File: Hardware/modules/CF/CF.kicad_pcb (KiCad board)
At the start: 4 copper layers, 83.3 x 68.2 mm, 20 parts, among them J1 CF Card, J2 Bus_PCI_6502, U1 74HC00, U2 74LS32, U3 74HCT74, U4 74HC138

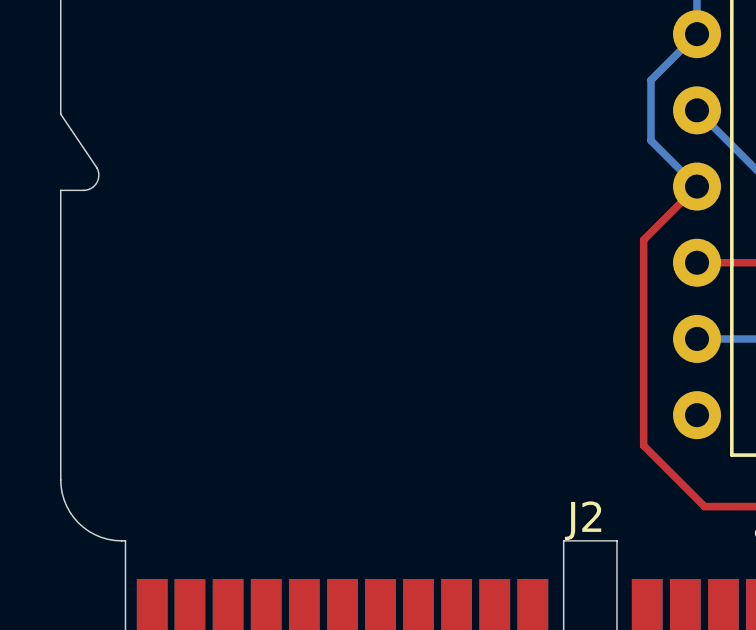
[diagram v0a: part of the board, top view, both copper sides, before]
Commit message: Hardware Review Pt. 1 fix Address Decoding for Strobe Generators add bulk capacitance to every board fix wiring of Prototyping Board
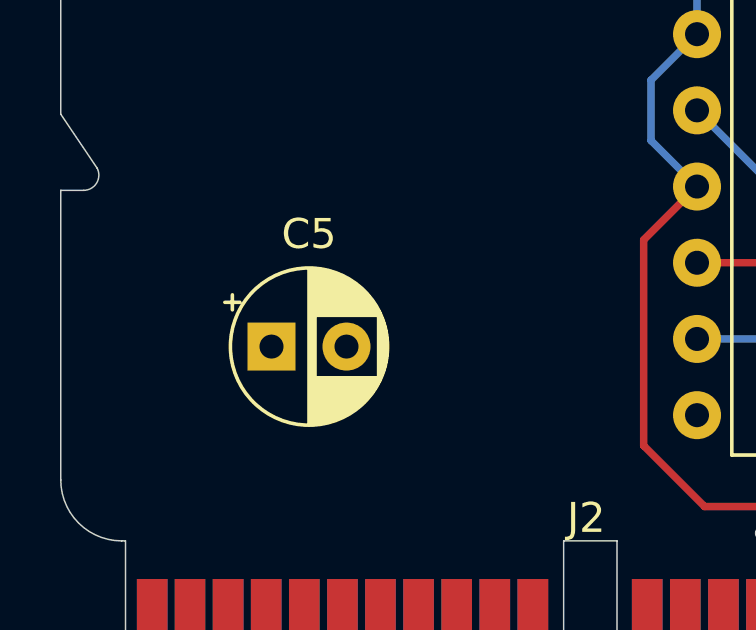
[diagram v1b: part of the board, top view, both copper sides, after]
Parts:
- added C5: C_Polarized, Capacitor_THT:CP_Radial_D5.0mm_P2.50mm, F.Cu at (106.5, 112.3)
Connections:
- J2 pad A11: /A13 -> unconnected-(J2-A13-PadA11)_0
- J2 pad A12: /A15 -> unconnected-(J2-A15-PadA12)
- J2 pad A25: /~{ROM} -> unconnected-(J2-~{ROM}-PadA25)_0
- J2 pad A27: /~{IRQ_0.0} -> unconnected-(J2-~{IRQ_0.0}-PadA27)_0
- J2 pad A28: /~{IRQ_0.1} -> unconnected-(J2-~{IRQ_0.1}-PadA28)_0
- J2 pad A29: /~{IRQ_0.2} -> unconnected-(J2-~{IRQ_0.2}-PadA29)_0
- J2 pad A30: /~{IRQ_0.3} -> unconnected-(J2-~{IRQ_0.3}-PadA30)_0
- J2 pad A31: /~{IRQ_0.4} -> unconnected-(J2-~{IRQ_0.4}-PadA31)_0
- J2 pad A32: /~{IRQ_0.5} -> unconnected-(J2-~{IRQ_0.5}-PadA32)_0
- J2 pad A33: /~{IRQ_0.6} -> unconnected-(J2-~{IRQ_0.6}-PadA33)
- J2 pad A34: /~{IRQ_0.7} -> unconnected-(J2-~{IRQ_0.7}-PadA34)
- J2 pad A38: /SYNC_VPA -> unconnected-(J2-Sync/VPA-PadA38)_0
- J2 pad A39: /Ø2/VDA -> unconnected-(J2-Ø2/VDA-PadA39)_0
- J2 pad A41: /~{RDY} -> unconnected-(J2-~{RDY}-PadA41)
- J2 pad A42: /~{BE} -> unconnected-(J2-~{BE}-PadA42)
- J2 pad A45: /E -> unconnected-(J2-E-PadA45)_0
- J2 pad A53: /RAM_0 -> unconnected-(J2-RAM0-PadA53)_0
- J2 pad A54: /RAM_1 -> unconnected-(J2-RAM1-PadA54)
- J2 pad A55: /RAM_2 -> unconnected-(J2-RAM2-PadA55)_0
- J2 pad A56: /RAM_3 -> unconnected-(J2-RAM3-PadA56)
- J2 pad A58: /RAM_4 -> unconnected-(J2-RAM4-PadA58)_0
- J2 pad A59: /RAM_5 -> unconnected-(J2-RAM5-PadA59)
- J2 pad A60: /RAM_6 -> unconnected-(J2-RAM6-PadA60)_0
- J2 pad A61: /RAM_7 -> unconnected-(J2-RAM7-PadA61)
- J2 pad A8: /A9 -> unconnected-(J2-A9-PadA8)_0
- J2 pad A9: /A11 -> unconnected-(J2-A11-PadA9)_0
- J2 pad B11: /A12 -> unconnected-(J2-A12-PadB11)
- J2 pad B12: /A14 -> unconnected-(J2-A14-PadB12)
- J2 pad B24: /~{L_RAM} -> unconnected-(J2-~{L_RAM}-PadB24)_0
- J2 pad B25: /~{H_RAM} -> unconnected-(J2-~{H_RAM}-PadB25)_0
- J2 pad B27: /~{IRQ} -> unconnected-(J2-~{IRQ}-PadB27)
- J2 pad B28: /~{IRQ_0} -> unconnected-(J2-~{IRQ_0}-PadB28)_0
- J2 pad B29: /~{IRQ_1} -> unconnected-(J2-~{IRQ_1}-PadB29)
- J2 pad B30: /~{IRQ_2} -> unconnected-(J2-~{IRQ_2}-PadB30)
- J2 pad B31: /~{IRQ_3} -> unconnected-(J2-~{IRQ_3}-PadB31)
- J2 pad B32: /~{IRQ_4} -> unconnected-(J2-~{IRQ_4}-PadB32)_0
- J2 pad B33: /~{NMI} -> unconnected-(J2-~{NMI}-PadB33)
- J2 pad B34: /PAGE -> unconnected-(J2-PAGE_ROM-PadB34)_0
- J2 pad B38: /~{VP} -> unconnected-(J2-~{VP}-PadB38)_0
- J2 pad B39: /~{ML} -> unconnected-(J2-~{ML}-PadB39)
- J2 pad B46: /M/X -> unconnected-(J2-M/~{X}-PadB46)_0
- J2 pad B53: /ROM_0 -> unconnected-(J2-ROM0-PadB53)_0
- J2 pad B54: /ROM_1 -> unconnected-(J2-ROM1-PadB54)
- J2 pad B55: /ROM_2 -> unconnected-(J2-ROM2-PadB55)
- J2 pad B56: /ROM_3 -> unconnected-(J2-ROM3-PadB56)
- J2 pad B58: /ROM_4 -> unconnected-(J2-ROM4-PadB58)
- J2 pad B59: /ROM_5 -> unconnected-(J2-ROM5-PadB59)_0
- J2 pad B60: /ROM_6 -> unconnected-(J2-ROM6-PadB60)
- J2 pad B61: /ROM_7 -> unconnected-(J2-ROM7-PadB61)_0
- J2 pad B8: /A8 -> unconnected-(J2-A8-PadB8)_0
- J2 pad B9: /A10 -> unconnected-(J2-A10-PadB9)_0
- U4 pad 15: /PORT_128 -> unconnected-(U4-~{Y0}-Pad15)

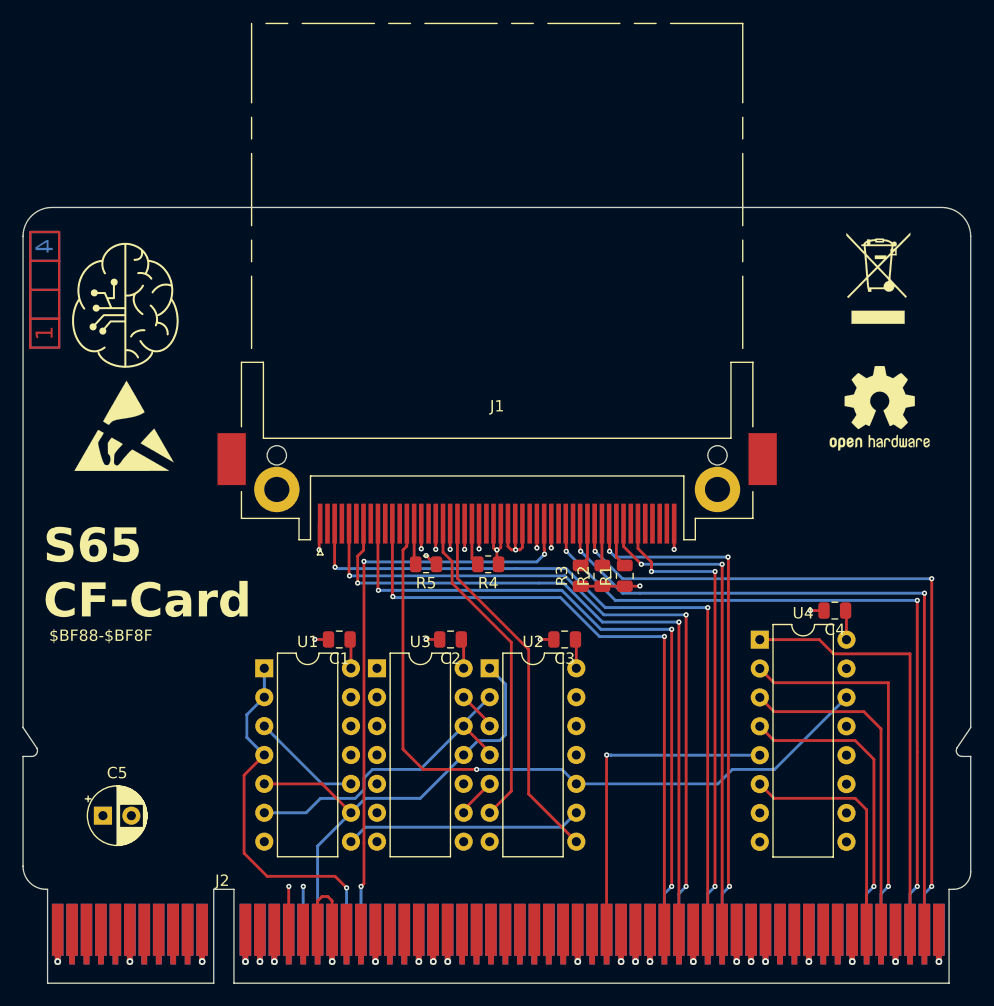
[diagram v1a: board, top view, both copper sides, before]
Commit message: Big Review Update - Changed Copper Pours on all PCBs - Implemented errors found at review - fixed some additional errors
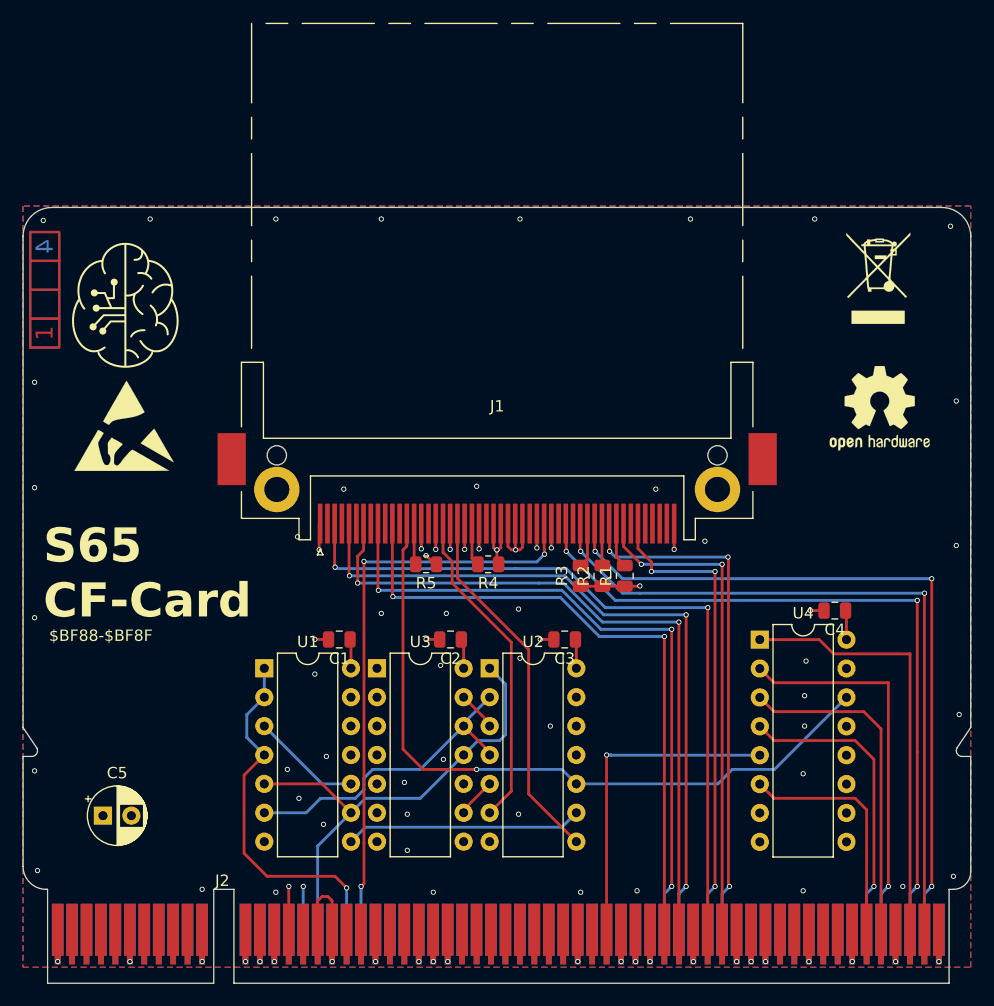
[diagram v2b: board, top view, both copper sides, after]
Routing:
- net +5V: vias 7 -> 56
- added copper zone on B.Cu, net +5V
- added copper zone on F.Cu, net +5V
- added copper zone on In2.Cu, net GND
- removed copper zone on In2.Cu, net +5V
